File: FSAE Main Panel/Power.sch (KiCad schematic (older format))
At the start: 18 parts

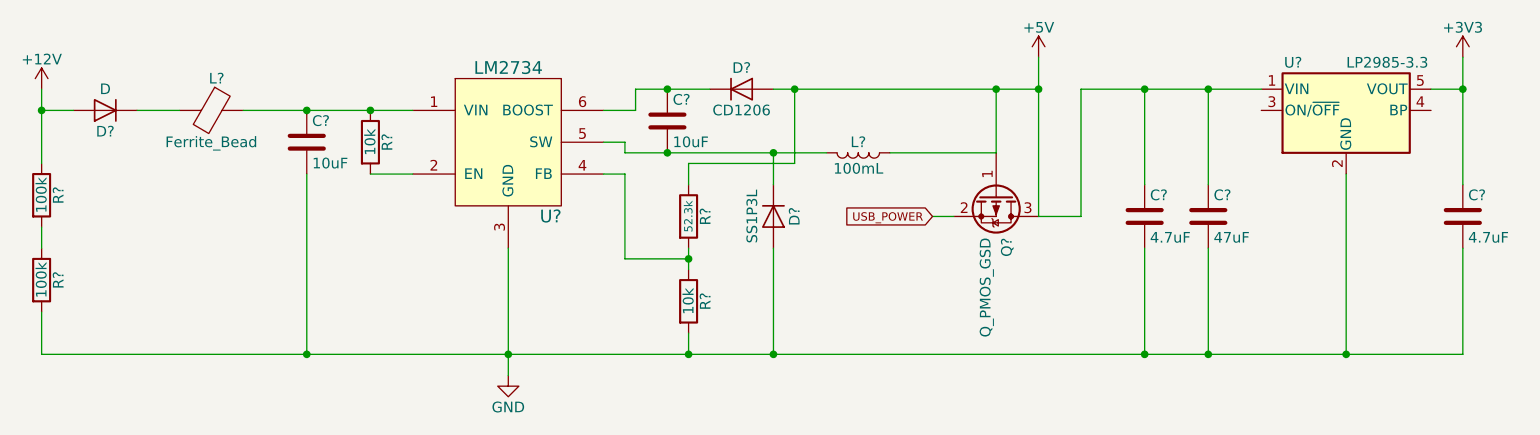
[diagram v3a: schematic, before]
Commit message: Added RPM LED Control
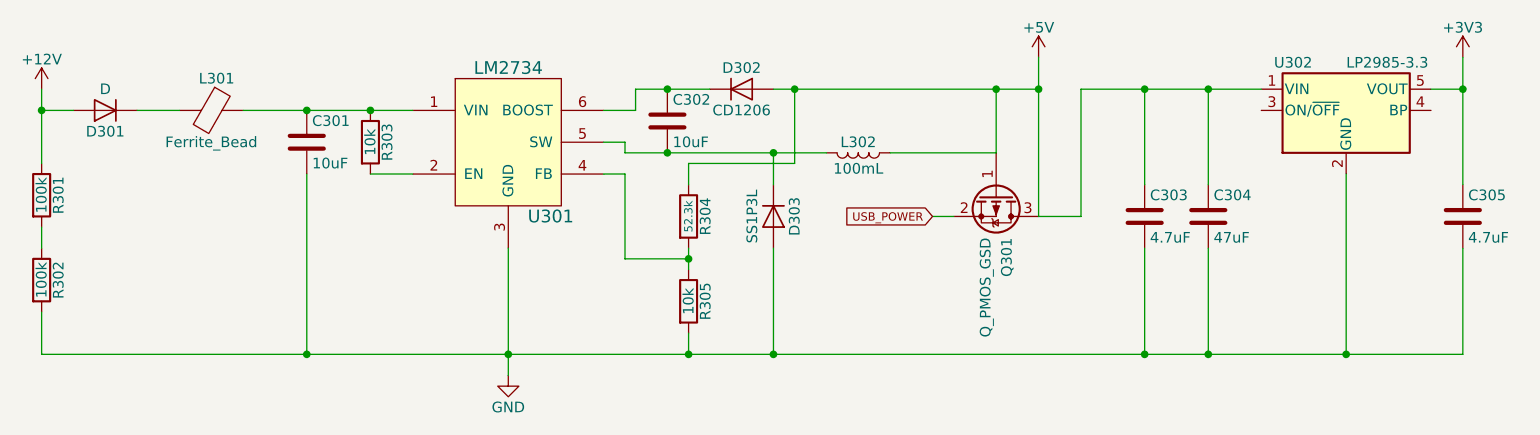
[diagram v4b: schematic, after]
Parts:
- gave numbers to parts that had none: 18
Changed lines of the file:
@@
 LIBS:contrib
 LIBS:valves
+LIBS:TI_Additions
+LIBS:apa102c
+LIBS:KingBright_Addition
+LIBS:lm2734
+LIBS:prtr5v0u2x
+LIBS:samd21g18a-au
 LIBS:FSAE Main Panel-cache
 EELAYER 25 0
@@
 $EndDescr
 $Comp
-L +12V #PWR?
+L +12V #PWR301
 U 1 1 5BD92350
 P 2350 3300
-F 0 "#PWR?" H 2350 3150 50  0001 C CNN
+F 0 "#PWR301" H 2350 3150 50  0001 C CNN
 F 1 "+12V" H 2350 3440 50  0000 C CNN
 F 2 "" H 2350 3300 50  0001 C CNN
@@
 $EndComp
 $Comp
-L D D?
+L D D301
 U 1 1 5BD92356
 P 2650 3400
-F 0 "D?" H 2650 3500 50  0000 C CNN
+F 0 "D301" H 2650 3500 50  0000 C CNN
 F 1 "D" H 2650 3300 50  0000 C CNN
 F 2 "" H 2650 3400 50  0001 C CNN
@@
 $EndComp
 $Comp
-L Ferrite_Bead L?
+L Ferrite_Bead L301
 U 1 1 5BD9235D
 P 3150 3400
-F 0 "L?" V 3000 3425 50  0000 C CNN
+F 0 "L301" V 3000 3425 50  0000 C CNN
 F 1 "Ferrite_Bead" V 3300 3400 50  0000 C CNN
 F 2 "" V 3080 3400 50  0001 C CNN
@@
 $EndComp
 $Comp
-L LM2734 U?
+L LM2734 U301
 U 1 1 5BD92364
 P 4550 3550
-F 0 "U?" H 4750 3200 60  0000 C CNN
+F 0 "U301" H 4750 3200 60  0000 C CNN
 F 1 "LM2734" H 4550 3900 60  0000 C CNN
 F 2 "" H 4550 3550 60  0001 C CNN
@@
 $EndComp
 $Comp
-L C C?
+L C C301
 U 1 1 5BD9236B
 P 3600 3550
-F 0 "C?" H 3625 3650 50  0000 L CNN
+F 0 "C301" H 3625 3650 50  0000 L CNN
 F 1 "10uF" H 3625 3450 50  0000 L CNN
 F 2 "" H 3638 3400 50  0001 C CNN
@@
 $EndComp
 $Comp
-L GND #PWR?
+L GND #PWR302
 U 1 1 5BD92372
 P 4550 4650
-F 0 "#PWR?" H 4550 4400 50  0001 C CNN
+F 0 "#PWR302" H 4550 4400 50  0001 C CNN
 F 1 "GND" H 4550 4500 50  0000 C CNN
 F 2 "" H 4550 4650 50  0001 C CNN
@@
 $EndComp
 $Comp
-L R R?
+L R R303
 U 1 1 5BD92378
 P 3900 3550
-F 0 "R?" V 3980 3550 50  0000 C CNN
+F 0 "R303" V 3980 3550 50  0000 C CNN
 F 1 "10k" V 3900 3550 50  0000 C CNN
 F 2 "" V 3830 3550 50  0001 C CNN
@@
 $EndComp
 $Comp
-L C C?
+L C C302
 U 1 1 5BD9237F
 P 5300 3450
-F 0 "C?" H 5325 3550 50  0000 L CNN
+F 0 "C302" H 5325 3550 50  0000 L CNN
 F 1 "10uF" H 5325 3350 50  0000 L CNN
 F 2 "" H 5338 3300 50  0001 C CNN
@@
 $EndComp
 $Comp
-L D D?
+L D D302
 U 1 1 5BD92386
 P 5650 3300
-F 0 "D?" H 5650 3400 50  0000 C CNN
+F 0 "D302" H 5650 3400 50  0000 C CNN
 F 1 "CD1206" H 5650 3200 50  0000 C CNN
 F 2 "" H 5650 3300 50  0001 C CNN
@@
 $EndComp
 $Comp
-L L L?
+L L L302
 U 1 1 5BD9238D
 P 6200 3600
-F 0 "L?" V 6150 3600 50  0000 C CNN
+F 0 "L302" V 6150 3600 50  0000 C CNN
 F 1 "100mL" V 6275 3600 50  0000 C CNN
 F 2 "" H 6200 3600 50  0001 C CNN
@@
 $EndComp
 $Comp
-L R R?
+L R R304
 U 1 1 5BD92394
 P 5400 3900
-F 0 "R?" V 5480 3900 50  0000 C CNN
+F 0 "R304" V 5480 3900 50  0000 C CNN
 F 1 "52.3k" V 5400 3900 39  0000 C CNN
 F 2 "" V 5330 3900 50  0001 C CNN
@@
 $EndComp
 $Comp
-L R R?
+L R R305
 U 1 1 5BD9239B
 P 5400 4300
-F 0 "R?" V 5480 4300 50  0000 C CNN
+F 0 "R305" V 5480 4300 50  0000 C CNN
 F 1 "10k" V 5400 4300 50  0000 C CNN
 F 2 "" V 5330 4300 50  0001 C CNN
@@
 $EndComp
 $Comp
-L D D?
+L D D303
 U 1 1 5BD923A2
 P 5800 3900
-F 0 "D?" H 5800 4000 50  0000 C CNN
+F 0 "D303" H 5800 4000 50  0000 C CNN
 F 1 "SS1P3L" H 5800 3800 50  0000 C CNN
 F 2 "" H 5800 3900 50  0001 C CNN
@@
 $EndComp
 $Comp
-L +5V #PWR?
+L +5V #PWR303
 U 1 1 5BD923A9
 P 7050 3150
-F 0 "#PWR?" H 7050 3000 50  0001 C CNN
+F 0 "#PWR303" H 7050 3000 50  0001 C CNN
 F 1 "+5V" H 7050 3290 50  0000 C CNN
 F 2 "" H 7050 3150 50  0001 C CNN
@@
 $EndComp
 $Comp
-L LP2985-3.3 U?
+L LP2985-3.3 U302
 U 1 1 5BD923AF
 P 8500 3400
-F 0 "U?" H 8250 3625 50  0000 C CNN
+F 0 "U302" H 8250 3625 50  0000 C CNN
 F 1 "LP2985-3.3" H 8500 3625 50  0000 L CNN
 F 2 "TO_SOT_Packages_SMD:SOT-23-5" H 8500 3725 50  0001 C CNN
@@
 $EndComp
 $Comp
-L C C?
+L C C303
 U 1 1 5BD923B6
 P 7550 3900
-F 0 "C?" H 7575 4000 50  0000 L CNN
+F 0 "C303" H 7575 4000 50  0000 L CNN
 F 1 "4.7uF" H 7575 3800 50  0000 L CNN
 F 2 "" H 7588 3750 50  0001 C CNN
@@
 $EndComp
 $Comp
-L C C?
+L C C304
 U 1 1 5BD923BD
 P 7850 3900
-F 0 "C?" H 7875 4000 50  0000 L CNN
+F 0 "C304" H 7875 4000 50  0000 L CNN
 F 1 "47uF" H 7875 3800 50  0000 L CNN
 F 2 "" H 7888 3750 50  0001 C CNN
@@
 	7550 4550 7550 4050
 $Comp
-L C C?
+L C C305
 U 1 1 5BD92405
 P 9050 3900
-F 0 "C?" H 9075 4000 50  0000 L CNN
+F 0 "C305" H 9075 4000 50  0000 L CNN
 F 1 "4.7uF" H 9075 3800 50  0000 L CNN
 F 2 "" H 9088 3750 50  0001 C CNN
@@
 Connection ~ 8500 4550
 $Comp
-L +3V3 #PWR?
+L +3V3 #PWR304
 U 1 1 5BD92411
 P 9050 3150
-F 0 "#PWR?" H 9050 3000 50  0001 C CNN
+F 0 "#PWR304" H 9050 3000 50  0001 C CNN
 F 1 "+3V3" H 9050 3290 50  0000 C CNN
 F 2 "" H 9050 3150 50  0001 C CNN
@@
 Connection ~ 9050 3300
 $Comp
-L R R?
+L R R301
 U 1 1 5BD925EB
 P 2350 3800
-F 0 "R?" V 2430 3800 50  0000 C CNN
+F 0 "R301" V 2430 3800 50  0000 C CNN
 F 1 "100k" V 2350 3800 50  0000 C CNN
 F 2 "" V 2280 3800 50  0001 C CNN
@@
 $EndComp
 $Comp
-L R R?
+L R R302
 U 1 1 5BD9273C
 P 2350 4200
-F 0 "R?" V 2430 4200 50  0000 C CNN
+F 0 "R302" V 2430 4200 50  0000 C CNN
 F 1 "100k" V 2350 4200 50  0000 C CNN
 F 2 "" V 2280 4200 50  0001 C CNN
@@
 Connection ~ 3600 4550
 $Comp
-L Q_PMOS_GSD Q?
+L Q_PMOS_GSD Q301
 U 1 1 5BD96D6D
 P 6850 3800
-F 0 "Q?" H 7050 3850 50  0000 L CNN
+F 0 "Q301" H 7050 3850 50  0000 L CNN
 F 1 "Q_PMOS_GSD" H 7050 3750 50  0000 L CNN
 F 2 "" H 7050 3900 50  0001 C CNN

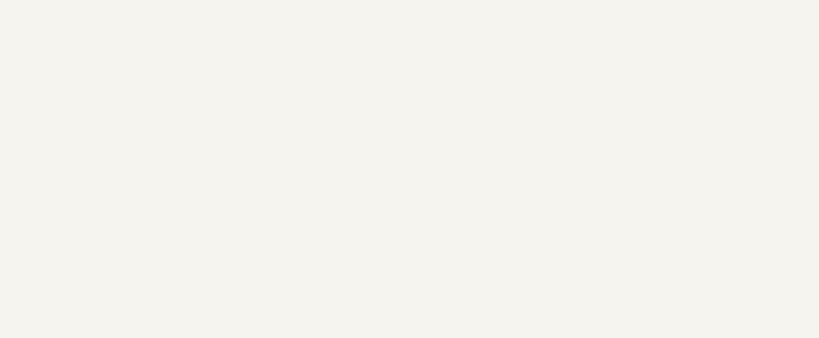
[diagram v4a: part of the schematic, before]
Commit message: Finished most LEDs, begun power regulators
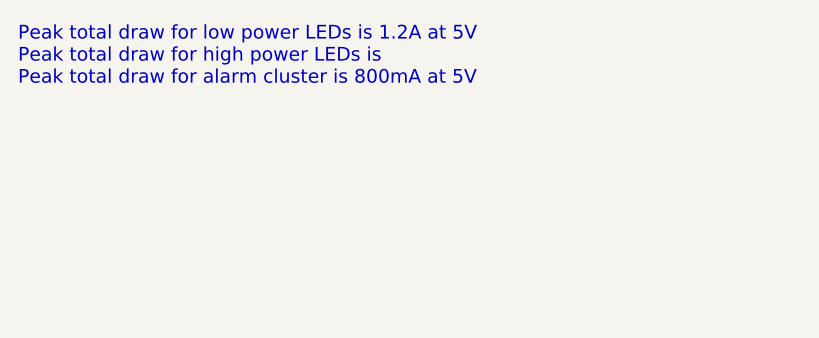
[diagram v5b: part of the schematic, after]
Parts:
- U301: footprint (none) -> TO_SOT_Packages_SMD:SOT-23-6; Output Current (none) -> 1A; Output Voltage (none) -> 0.8-18V
- U302: Manufacturer (none) -> TI; Output Current (none) -> 150mA; Output Voltage (none) -> 3.3V
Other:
- note added: "Peak total draw for low power LEDs is 1.2A at 5V\nPeak total draw for high power LEDs is \nPeak total draw for alarm cluster is 800mA at 5V"
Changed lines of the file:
@@
 F 0 "U301" H 4750 3200 60  0000 C CNN
 F 1 "LM2734" H 4550 3900 60  0000 C CNN
-F 2 "" H 4550 3550 60  0001 C CNN
-F 3 "" H 4550 3550 60  0001 C CNN
+F 2 "TO_SOT_Packages_SMD:SOT-23-6" H 4550 3550 60  0001 C CNN
+F 3 "http://www.ti.com/lit/ds/symlink/lm2734.pdf" H 4550 3550 60  0001 C CNN
+F 4 "0.8-18V" H 4550 3550 60  0001 C CNN "Output Voltage"
+F 5 "1A" H 4550 3550 60  0001 C CNN "Output Current"
 	1    4550 3550
 	1    0    0    -1
@@
 F 1 "LP2985-3.3" H 8500 3625 50  0000 L CNN
 F 2 "TO_SOT_Packages_SMD:SOT-23-5" H 8500 3725 50  0001 C CNN
-F 3 "" H 8500 3400 50  0001 C CNN
+F 3 "http://www.ti.com/lit/ds/symlink/lp2985-n.pdf" H 8500 3400 50  0001 C CNN
+F 4 "TI" H 8500 3400 60  0001 C CNN "Manufacturer"
+F 5 "3.3V" H 8500 3400 60  0001 C CNN "Output Voltage"
+F 6 "150mA" H 8500 3400 60  0001 C CNN "Output Current"
 	1    8500 3400
 	1    0    0    -1
@@
 Connection ~ 7050 3300
 Connection ~ 6850 3300
+Text Notes 600  850  0    60   ~ 0
+Peak total draw for low power LEDs is 1.2A at 5V\nPeak total draw for high power LEDs is \nPeak total draw for alarm cluster is 800mA at 5V
 $EndSCHEMATC

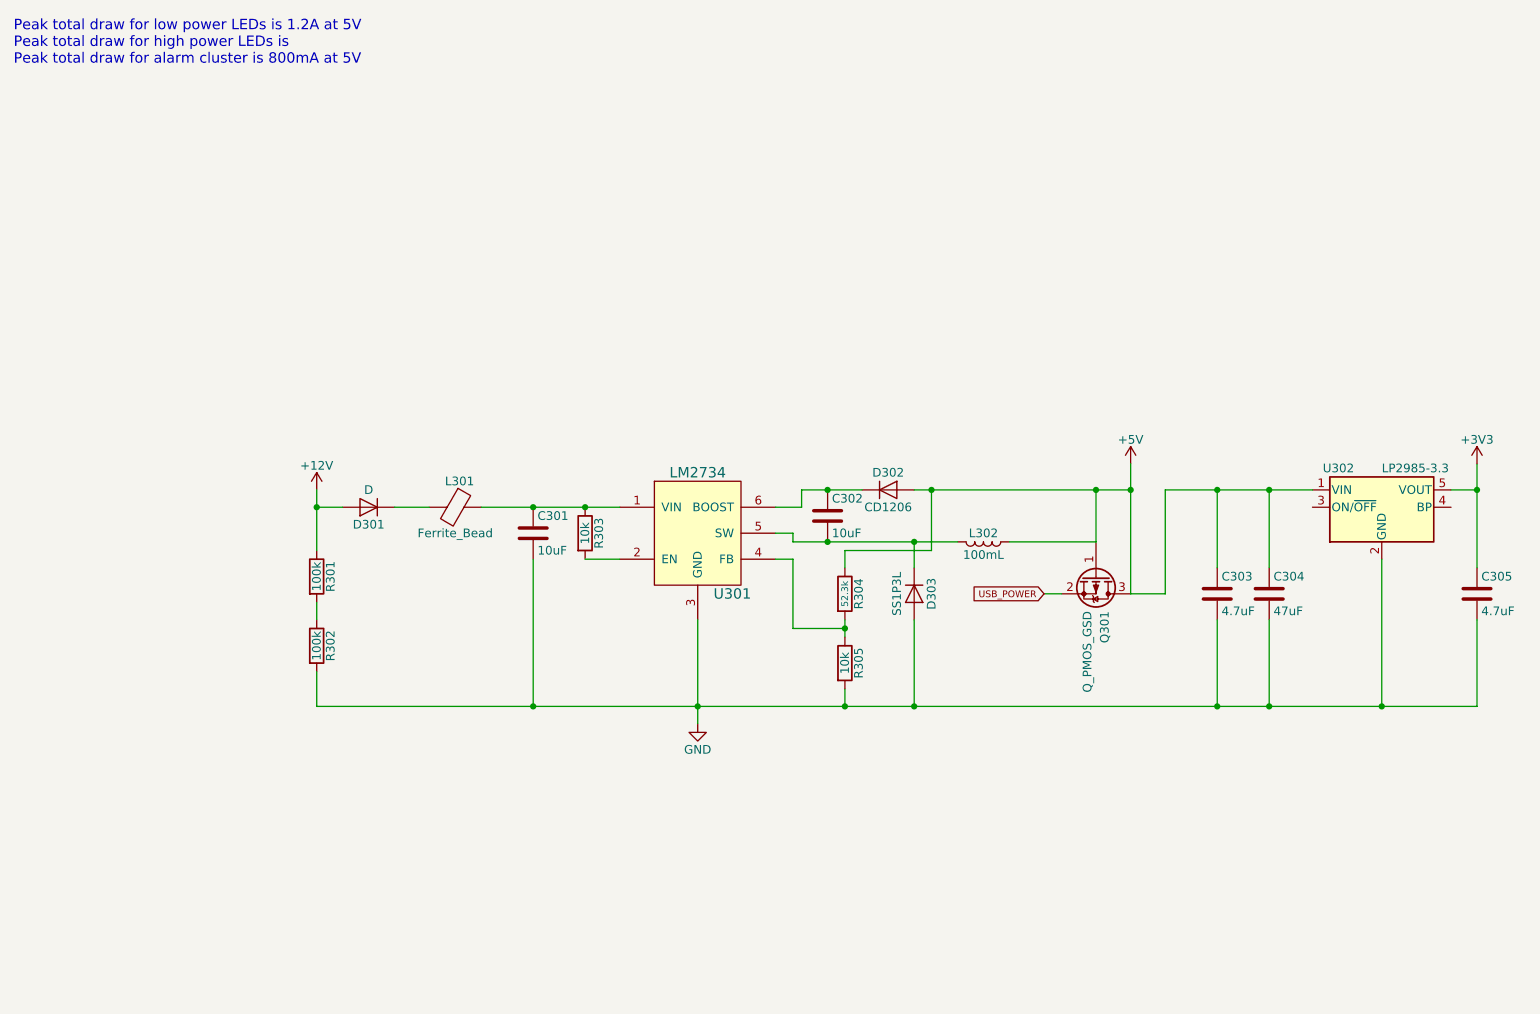
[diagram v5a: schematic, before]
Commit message: Moved USB connection to External_Interface
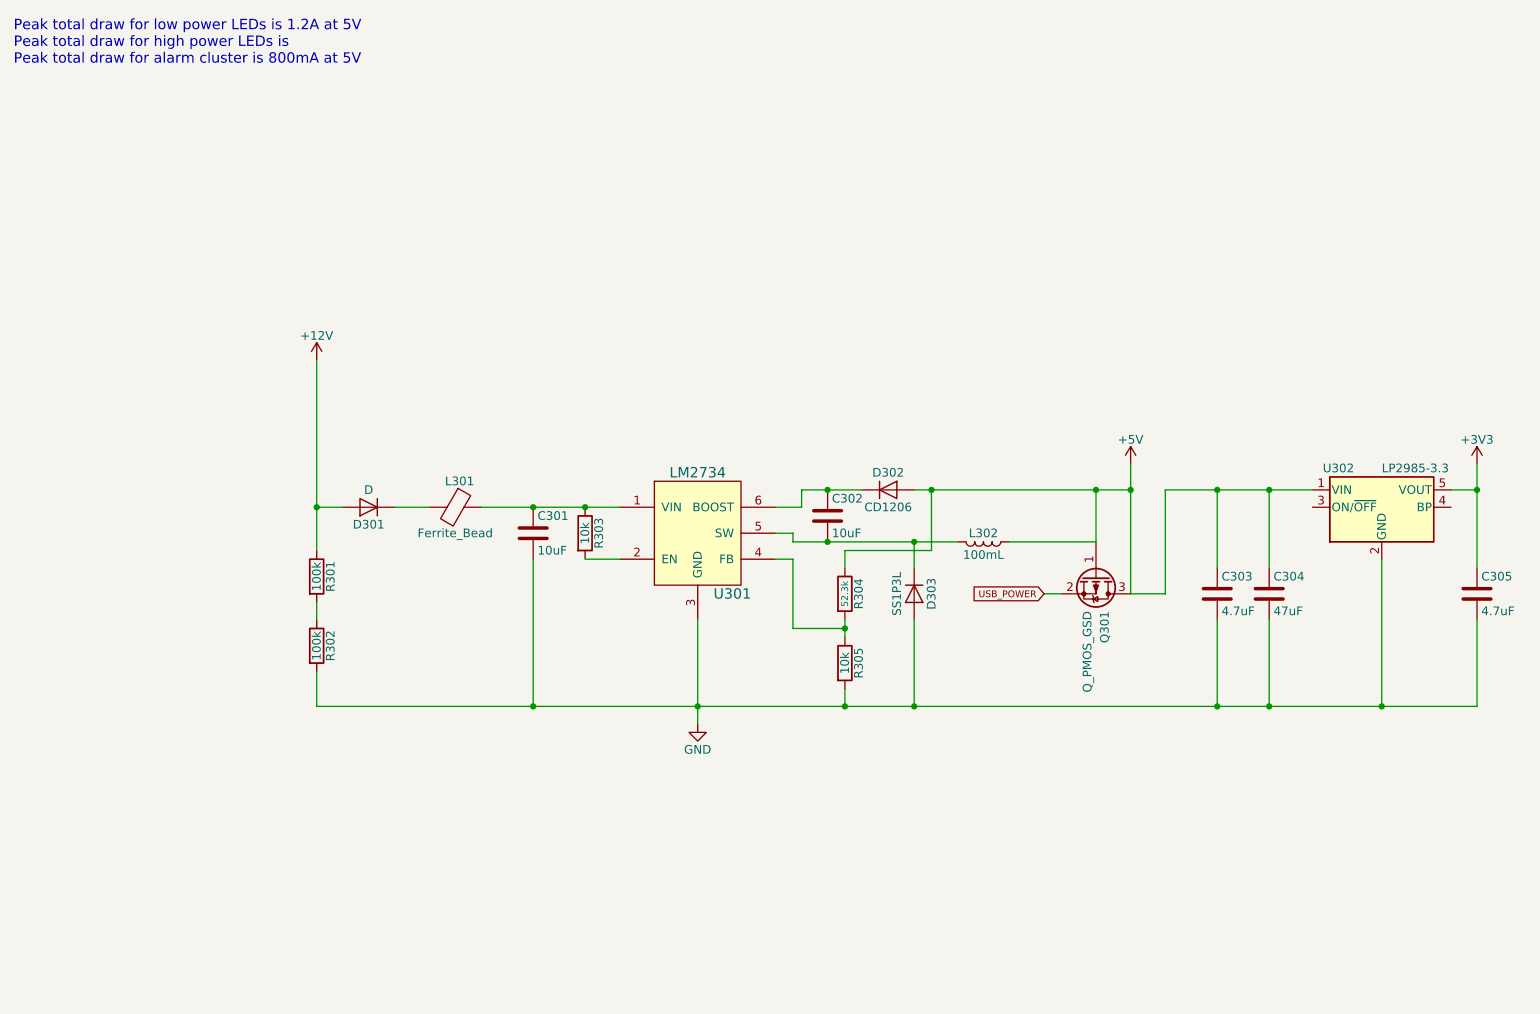
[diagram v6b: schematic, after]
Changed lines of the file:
@@
 L +12V #PWR301
 U 1 1 5BD92350
-P 2350 3300
-F 0 "#PWR301" H 2350 3150 50  0001 C CNN
-F 1 "+12V" H 2350 3440 50  0000 C CNN
-F 2 "" H 2350 3300 50  0001 C CNN
-F 3 "" H 2350 3300 50  0001 C CNN
-	1    2350 3300
+P 2350 2550
+F 0 "#PWR301" H 2350 2400 50  0001 C CNN
+F 1 "+12V" H 2350 2690 50  0000 C CNN
+F 2 "" H 2350 2550 50  0001 C CNN
+F 3 "" H 2350 2550 50  0001 C CNN
+	1    2350 2550
 	1    0    0    -1
 $EndComp
@@
 $EndComp
 Wire Wire Line
-	2350 3300 2350 3650
+	2350 2550 2350 3400
+Wire Wire Line
+	2350 3400 2350 3650
 Wire Wire Line
 	2350 3400 2500 3400
@@
 	2800 3400 3000 3400
 Wire Wire Line
-	3300 3400 4100 3400
+	3300 3400 3600 3400
+Wire Wire Line
+	3600 3400 3900 3400
+Wire Wire Line
+	3900 3400 4100 3400
 Connection ~ 3600 3400
 Connection ~ 3900 3400
@@
 	5100 4100 5400 4100
 Wire Wire Line
-	5400 4050 5400 4150
+	5400 4050 5400 4100
+Wire Wire Line
+	5400 4100 5400 4150
 Connection ~ 5400 4100
 Wire Wire Line
 	5400 4550 5400 4450
 Wire Wire Line
-	4550 4050 4550 4650
+	4550 4050 4550 4550
+Wire Wire Line
+	4550 4550 4550 4650
 Connection ~ 4550 4550
 Wire Wire Line
@@
 	5150 3400 5150 3300
 Wire Wire Line
-	5150 3300 5500 3300
+	5150 3300 5300 3300
+Wire Wire Line
+	5300 3300 5500 3300
 Wire Wire Line
 	5000 3550 5100 3550
@@
 	5100 3550 5100 3600
 Wire Wire Line
-	5100 3600 6050 3600
+	5100 3600 5300 3600
+Wire Wire Line
+	5300 3600 5800 3600
+Wire Wire Line
+	5800 3600 6050 3600
 Connection ~ 5300 3300
 Wire Wire Line
@@
 	8500 4550 8500 3700
 Wire Wire Line
-	2350 4550 9050 4550
+	2350 4550 3600 4550
+Wire Wire Line
+	3600 4550 4550 4550
+Wire Wire Line
+	4550 4550 5400 4550
+Wire Wire Line
+	5400 4550 5800 4550
+Wire Wire Line
+	5800 4550 7550 4550
+Wire Wire Line
+	7550 4550 7850 4550
+Wire Wire Line
+	7850 4550 8500 4550
+Wire Wire Line
+	8500 4550 9050 4550
 Connection ~ 7550 4550
 Connection ~ 7850 4550
@@
 	8900 3300 9050 3300
 Wire Wire Line
-	9050 3150 9050 3750
+	9050 3150 9050 3300
+Wire Wire Line
+	9050 3300 9050 3750
 Wire Wire Line
 	9050 4550 9050 4050
@@
 USB_POWER
 Wire Wire Line
-	5800 3300 7050 3300
+	5800 3300 5900 3300
+Wire Wire Line
+	5900 3300 6850 3300
+Wire Wire Line
+	6850 3300 7050 3300
 Wire Wire Line
 	6550 3900 6650 3900
@@
 	7250 3900 7250 3300
 Wire Wire Line
-	7250 3300 8100 3300
-Wire Wire Line
-	7050 3150 7050 3900
+	7250 3300 7550 3300
+Wire Wire Line
+	7550 3300 7850 3300
+Wire Wire Line
+	7850 3300 8100 3300
+Wire Wire Line
+	7050 3150 7050 3300
+Wire Wire Line
+	7050 3300 7050 3900
 Wire Wire Line
 	6850 3300 6850 3600
